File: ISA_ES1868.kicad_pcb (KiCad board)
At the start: 4 copper layers, 104.1 x 102.9 mm, 107 parts, among them J1 LINE IN, J10 Volume buttons, J11 ISA BUS, J2 MIC, J3 Joystick/MIDI, J5 Wavetable, J7 SPKR OUT, J8 LINE OUT, U1 L78L05_TO92, U2 74LS138, U3 ES1868F, U4 93LC66, U7 LM1877, Y1 14.318Mhz

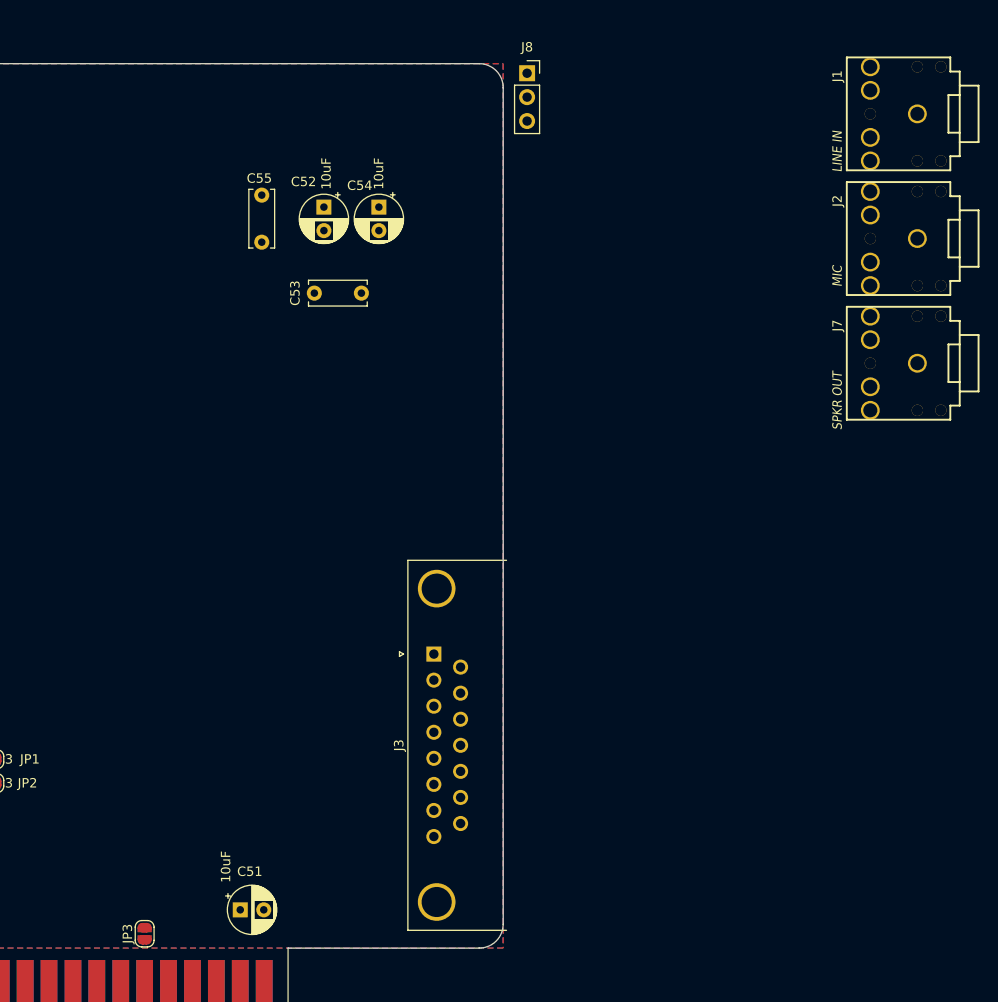
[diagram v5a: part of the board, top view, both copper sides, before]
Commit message: Organize external connectors
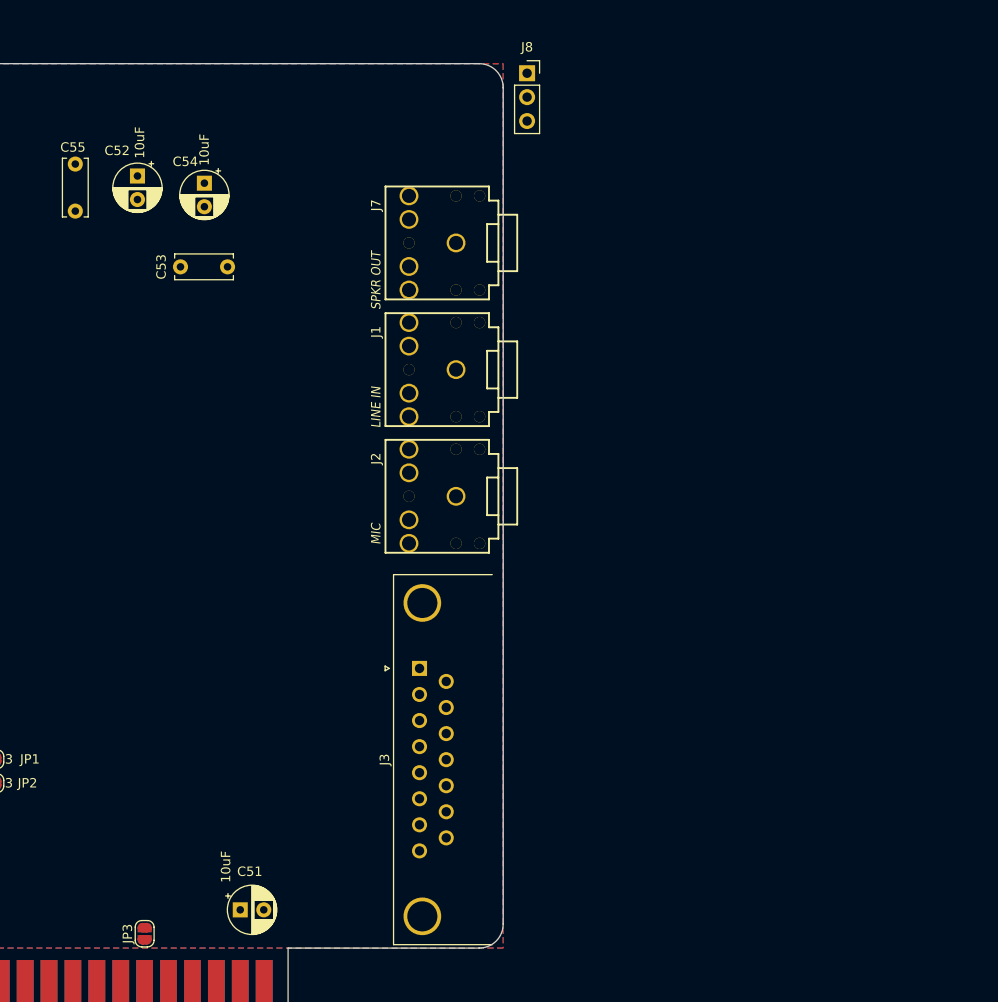
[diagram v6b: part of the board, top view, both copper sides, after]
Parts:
- moved J2 56.2 mm to (314.5, 146.3)
- moved J1 56.1 mm to (314.5, 132.8)
- moved J7 50.7 mm to (314.5, 119.4)
- moved C52 20.1 mm to (276.1, 112.3)
- moved C55 20.1 mm to (269.5, 111.0)
- moved C54 18.7 mm to (283.2, 113.0)
- moved C53 14.5 mm to (280.7, 121.9)
- moved J3 2.16 mm to (306.1, 164.6)
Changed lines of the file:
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@@
   (general
     (thickness 1.6)
-    (drawings 13)
+    (drawings 14)
     (tracks 0)
     (zones 0)
@@
   )
   (module My_Components:Conn_Audio_3.5mm_Stereo_SJ1-352XNG (layer F.Cu)
-    (at 363.474 132.164 270)
+    (at 314.452 119.38 270)
     (descr "Connector, Audio Stereo 3.5mm, CUI SJ1-352XNG")
     (tags "3.5MM STEREO AUDIO CONN CUI SJ1-352XNG")
@@
   )
   (module My_Components:Conn_Audio_3.5mm_Stereo_SJ1-352XNG (layer F.Cu)
-    (at 363.474 118.914 270)
+    (at 314.452 146.304 270)
     (descr "Connector, Audio Stereo 3.5mm, CUI SJ1-352XNG")
     (tags "3.5MM STEREO AUDIO CONN CUI SJ1-352XNG")
@@
   )
   (module My_Components:Conn_Audio_3.5mm_Stereo_SJ1-352XNG (layer F.Cu)
-    (at 363.474 105.664 270)
+    (at 314.452 132.842 270)
     (descr "Connector, Audio Stereo 3.5mm, CUI SJ1-352XNG")
     (tags "3.5MM STEREO AUDIO CONN CUI SJ1-352XNG")
@@
   )
   (module Connector_Dsub:DSUB-15_Female_Horizontal_P2.77x2.84mm_EdgePinOffset4.94mm_Housed_MountingHolesOffset7.48mm (layer F.Cu)
-    (at 307.594 163.068 90)
+    (at 306.07 164.592 90)
     (descr "15-pin D-Sub connector, horizontal/angled (90 deg), THT-mount, female, pitch 2.77x2.84mm, pin-PCB-offset 4.9399999999999995mm, distance of mounting holes 33.3mm, distance of mounting holes to PCB edge 7.4799999999999995mm, see https://disti-assets.s3.amazonaws.com/tonar/files/datasheets/16730.pdf")
     (tags "15-pin D-Sub connector horizontal angled 90deg THT female pitch 2.77x2.84mm pin-PCB-offset 4.9399999999999995mm mounting-holes-distance 33.3mm mounting-hole-offset 33.3mm")
@@
   )
   (module Capacitor_THT:C_Disc_D6.0mm_W2.5mm_P5.00mm (layer F.Cu)
-    (at 289.306 114.3 270)
+    (at 269.494 110.998 270)
     (descr "C, Disc series, Radial, pin pitch=5.00mm, , diameter*width=6*2.5mm^2, Capacitor, http://cdn-reichelt.de/documents/datenblatt/B300/DS_KERKO_TC.pdf")
     (tags "C Disc series Radial pin pitch 5.00mm  diameter 6mm width 2.5mm Capacitor")
@@
   )
   (module Capacitor_THT:CP_Radial_D5.0mm_P2.50mm (layer F.Cu)
-    (at 301.752 115.57 270)
+    (at 283.21 113.03 270)
     (descr "CP, Radial series, Radial, pin pitch=2.50mm, , diameter=5mm, Electrolytic Capacitor")
     (tags "CP Radial series Radial pin pitch 2.50mm  diameter 5mm Electrolytic Capacitor")
@@
   )
   (module Capacitor_THT:C_Disc_D6.0mm_W2.5mm_P5.00mm (layer F.Cu)
-    (at 294.894 124.714)
+    (at 280.67 121.92)
     (descr "C, Disc series, Radial, pin pitch=5.00mm, , diameter*width=6*2.5mm^2, Capacitor, http://cdn-reichelt.de/documents/datenblatt/B300/DS_KERKO_TC.pdf")
     (tags "C Disc series Radial pin pitch 5.00mm  diameter 6mm width 2.5mm Capacitor")
@@
   )
   (module Capacitor_THT:CP_Radial_D5.0mm_P2.50mm (layer F.Cu)
-    (at 295.91 115.57 270)
+    (at 276.098 112.268 270)
     (descr "CP, Radial series, Radial, pin pitch=2.50mm, , diameter=5mm, Electrolytic Capacitor")
     (tags "CP Radial series Radial pin pitch 2.50mm  diameter 5mm Electrolytic Capacitor")
@@
     )
   )
+  (dimension 8.636 (width 0.15) (layer Dwgs.User)
+    (gr_text "8,636 mm" (at 310.642 197.896) (layer Dwgs.User)
+      (effects (font (size 1 1) (thickness 0.15)))
+    )
+    (feature1 (pts (xy 306.324 191.008) (xy 306.324 197.182421)))
+    (feature2 (pts (xy 314.96 191.008) (xy 314.96 197.182421)))
+    (crossbar (pts (xy 314.96 196.596) (xy 306.324 196.596)))
+    (arrow1a (pts (xy 306.324 196.596) (xy 307.450504 196.009579)))
+    (arrow1b (pts (xy 306.324 196.596) (xy 307.450504 197.182421)))
+    (arrow2a (pts (xy 314.96 196.596) (xy 313.833496 196.009579)))
+    (arrow2b (pts (xy 314.96 196.596) (xy 313.833496 197.182421)))
+  )
   (gr_line (start 213.36 100.33) (end 312.42 100.33) (layer Edge.Cuts) (width 0.05))

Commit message: Begin organizing PCB
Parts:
- L1: value Ferrite Bead -> Filter
- moved R13 153.1 mm to (301.2, 180.6), turned to 180 degrees
- moved C3 148.5 mm to (234.9, 148.6)
- moved C2 143.0 mm to (237.0, 175.3)
- moved R3 137.2 mm to (301.2, 189.7), turned to 180 degrees
- moved C25 133.3 mm to (281.7, 171.4)
- moved R8 133.1 mm to (301.2, 177.5), turned to 180 degrees
- moved C20 130.3 mm to (294.9, 186.7)
- moved R9 126.2 mm to (301.2, 174.5), turned to 180 degrees
- moved R35 125.1 mm to (280.4, 180.6)
- moved R34 124.5 mm to (280.4, 168.4)
- moved C18 124.1 mm to (294.9, 192.8)
- moved C23 122.8 mm to (281.9, 165.4)
- moved R12 119.9 mm to (301.2, 171.4), turned to 180 degrees
- moved L1 115.9 mm to (280.9, 153.2)
- moved C24 115.6 mm to (281.7, 183.6)
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
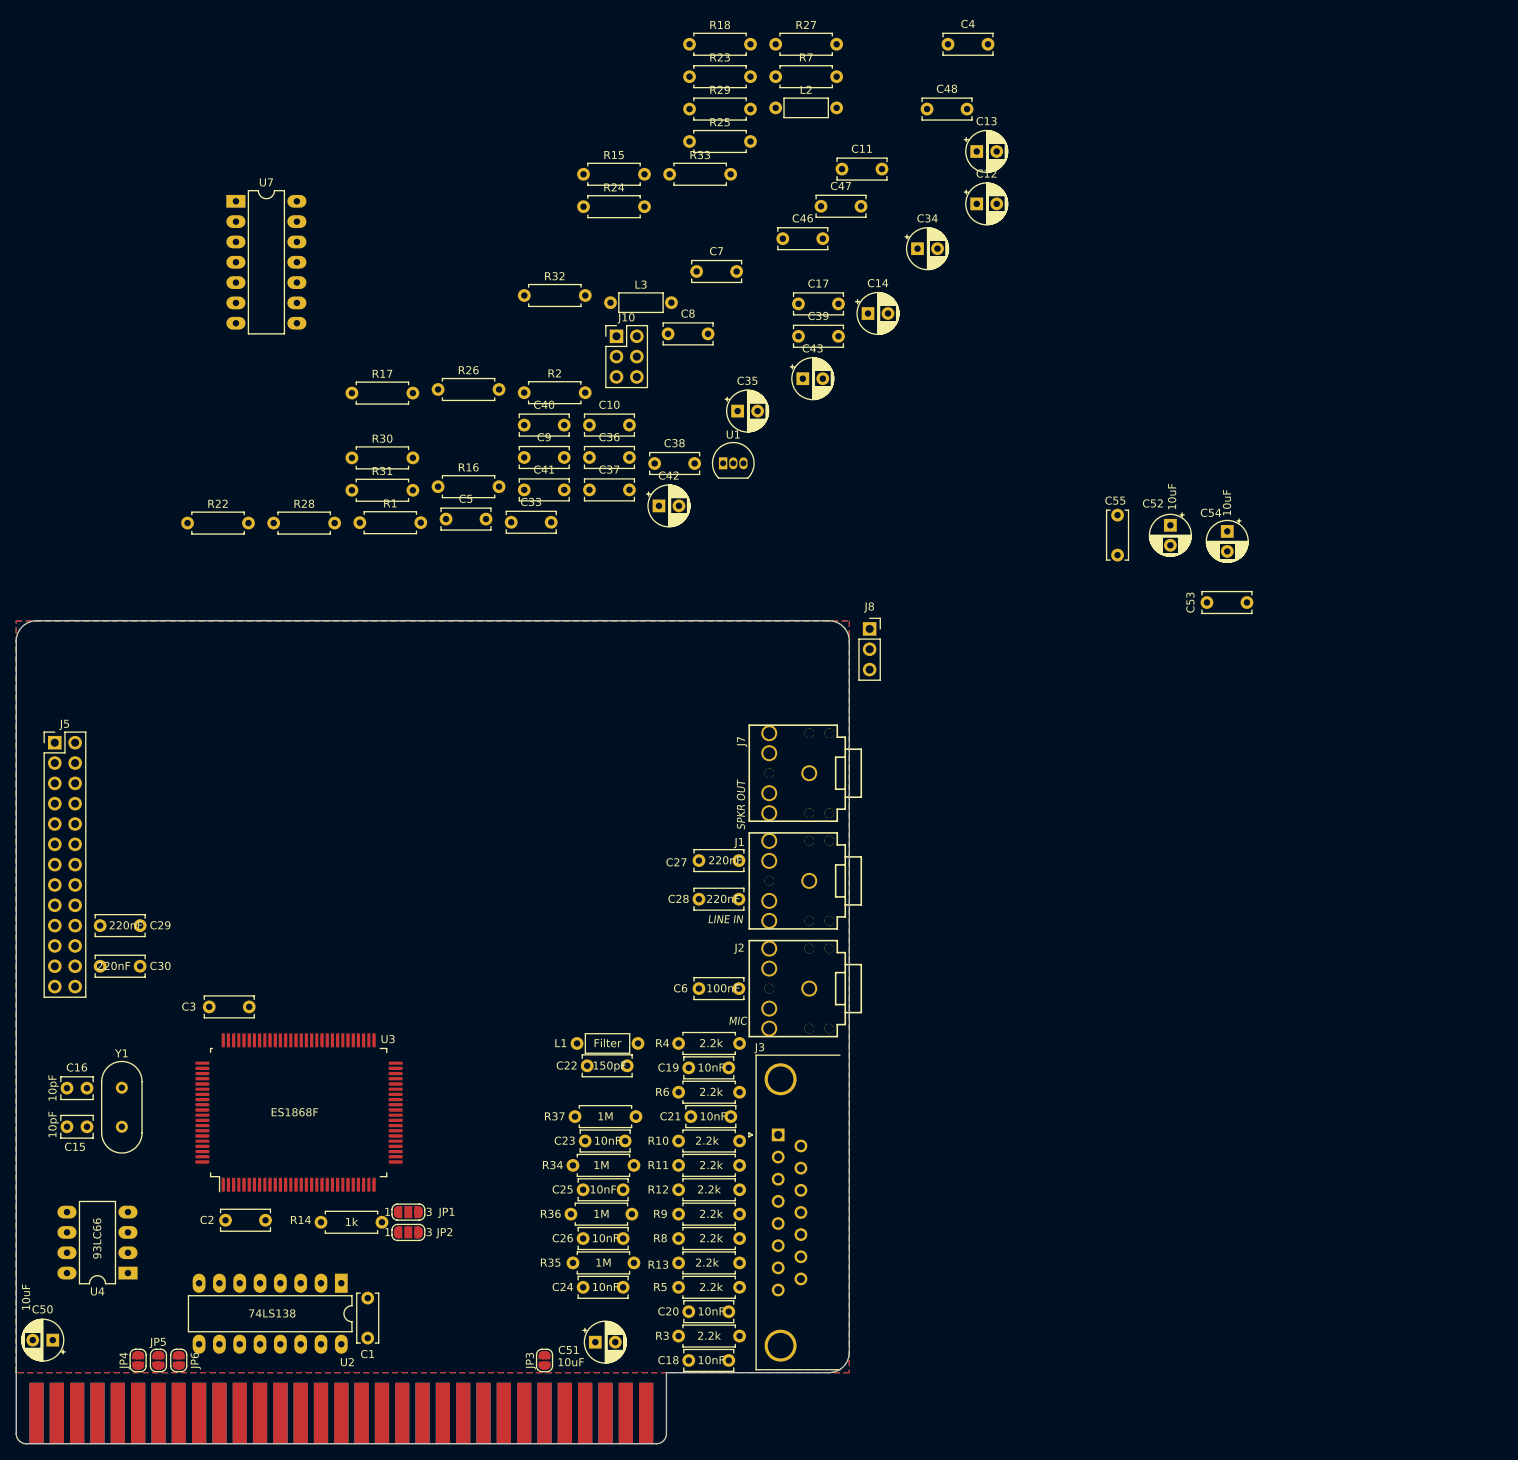
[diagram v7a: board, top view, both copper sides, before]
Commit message: More board component placement
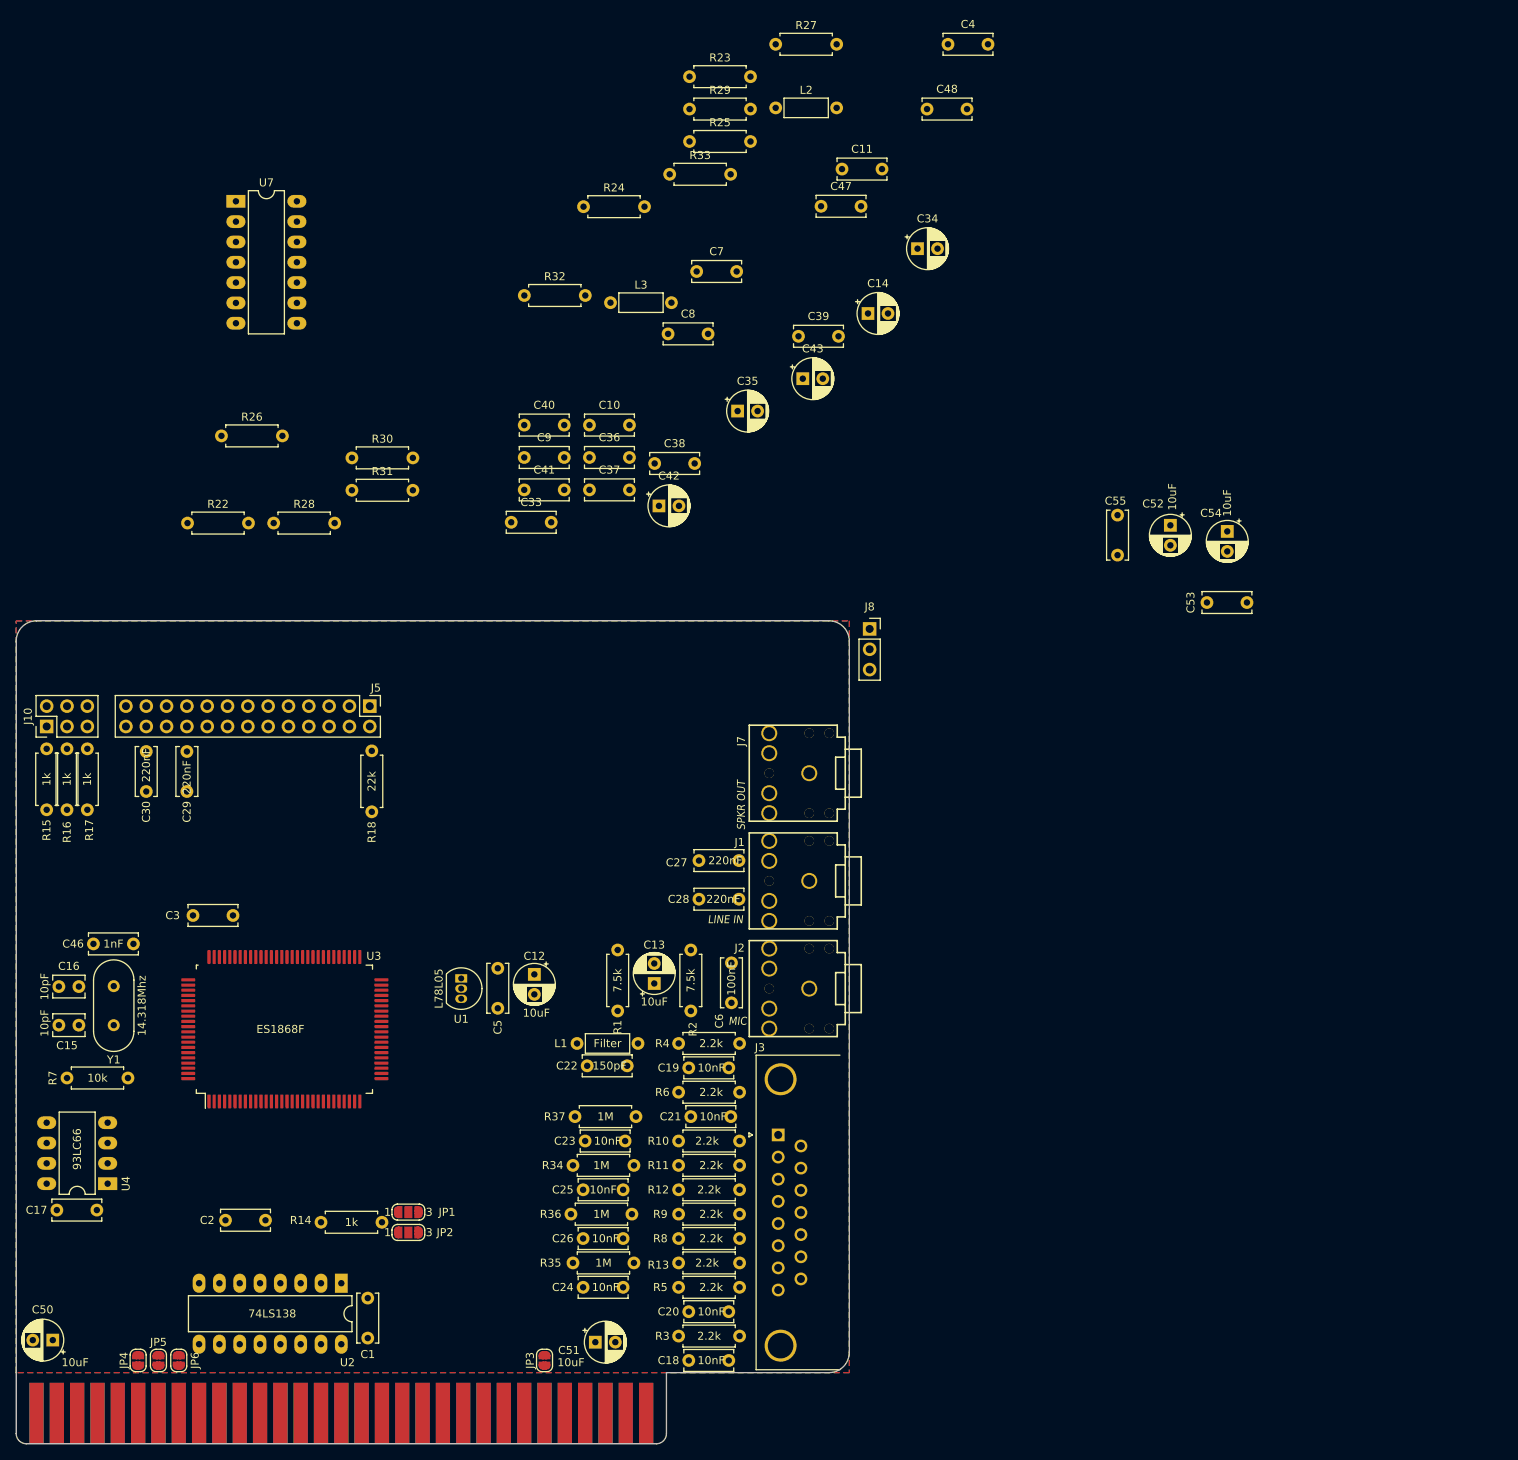
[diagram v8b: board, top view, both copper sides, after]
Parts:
- U1: value L78L05_TO92 -> L78L05
- moved R7 149.1 mm to (224.8, 157.5), turned to 180 degrees
- moved C17 143.3 mm to (220.9, 174.0), turned to 180 degrees
- moved C46 123.3 mm to (220.5, 140.7)
- moved C13 111.5 mm to (290.6, 145.7), turned to 90 degrees
- moved C12 111.1 mm to (275.6, 144.5), turned to 270 degrees
- moved R15 104.0 mm to (214.6, 124.0), turned to 90 degrees
- moved R18 96.8 mm to (255.3, 116.6), turned to 270 degrees
- moved J10 86.3 mm to (214.6, 113.5), turned to 90 degrees
- moved R2 80.0 mm to (295.1, 149.1), turned to 90 degrees
- moved U1 72.2 mm to (266.4, 145.0), turned to 270 degrees
- moved R1 62.4 mm to (286.0, 141.5), turned to 270 degrees
- moved R17 61.7 mm to (219.7, 124.0), turned to 90 degrees
- moved R16 61.5 mm to (217.2, 124.0), turned to 90 degrees
- moved C5 56.5 mm to (271.0, 143.8), turned to 270 degrees
- moved J5 39.6 mm to (255.0, 111.0), turned to 270 degrees
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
